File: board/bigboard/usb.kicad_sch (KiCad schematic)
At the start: 4 parts, among them J3 USB_C_Receptacle_USB2.0

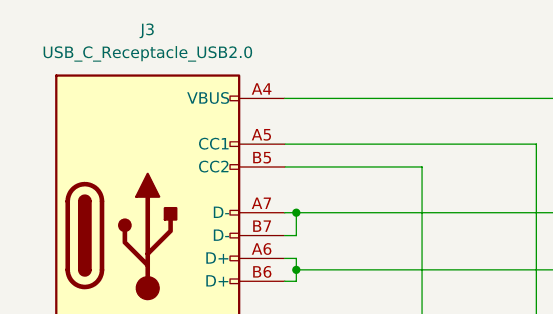
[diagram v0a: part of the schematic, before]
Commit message: Manufactured version of bigboard
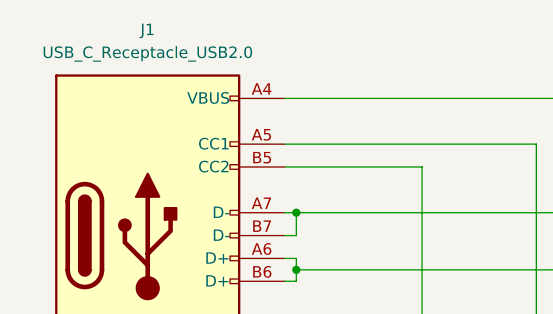
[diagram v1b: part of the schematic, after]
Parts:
- R4, R5: MPN (none) -> RC0201FR-075K1L
- renumbered J3 to J1
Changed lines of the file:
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@@
+      (effects (font (size 1.27 1.27)) hide)
+    )
+    (property "MPN" "RC0201FR-075K1L" (id 5) (at 137.16 110.49 0)
       (effects (font (size 1.27 1.27)) hide)
     )
@@
       (effects (font (size 1.27 1.27)) hide)
     )
+    (property "MPN" "RC0201FR-075K1L" (id 5) (at 124.46 110.49 0)
+      (effects (font (size 1.27 1.27)) hide)
+    )
     (pin "1")
     (pin "2")
@@
   (symbol (lib_id "Connector:USB_C_Receptacle_USB2.0") (at 93.98 93.98 0) (unit 1)
     (in_bom yes) (on_board yes) (fields_autoplaced)
-    (property "Reference" "J3" (id 0) (at 93.98 71.12 0))
+    (property "Reference" "J1" (id 0) (at 93.98 71.12 0))
     (property "Value" "USB_C_Receptacle_USB2.0" (id 1) (at 93.98 73.66 0))
     (property "Footprint" "Connector_USB:USB_C_Receptacle_XKB_U262-16XN-4BVC11" (id 2) (at 97.79 93.98 0)
@@
   (symbol (lib_id "power:GND") (at 86.36 127 0) (unit 1)
     (in_bom yes) (on_board yes) (fields_autoplaced)
-    (property "Reference" "#PWR08" (id 0) (at 86.36 133.35 0)
+    (property "Reference" "#PWR07" (id 0) (at 86.36 133.35 0)
       (effects (font (size 1.27 1.27)) hide)
     )

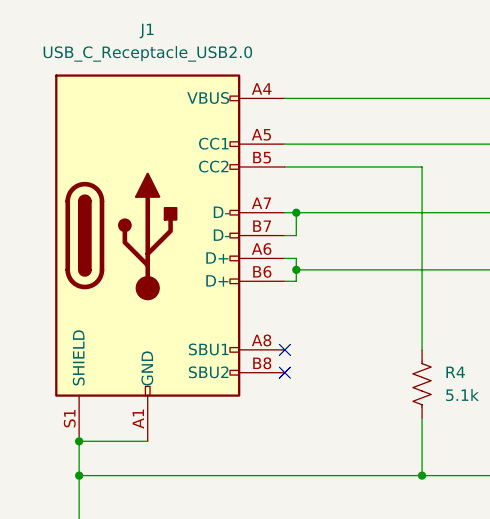
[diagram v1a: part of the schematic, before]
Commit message: Update board to kicad 7
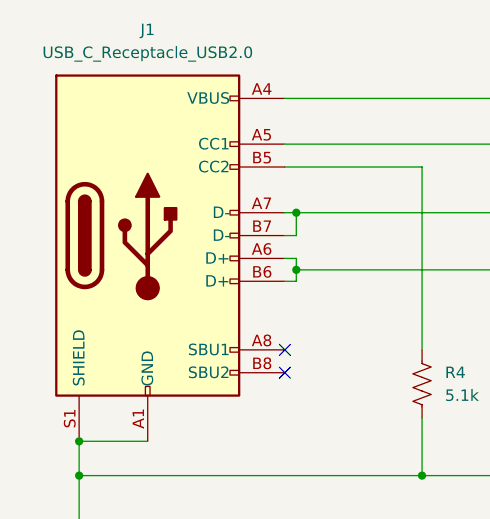
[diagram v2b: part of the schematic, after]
